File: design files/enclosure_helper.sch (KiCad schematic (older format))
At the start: 42 parts, among them J1 PSU_CON, J11 FLASH_JUMPER, J2 UART_CON, J3 LED_BTN, J4 FAN_CON, J5 PSU_BTN, J6 FAN_BTN, J7 POW_CON, J8 LED_FAN_POW_CON, J9 LED_CON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

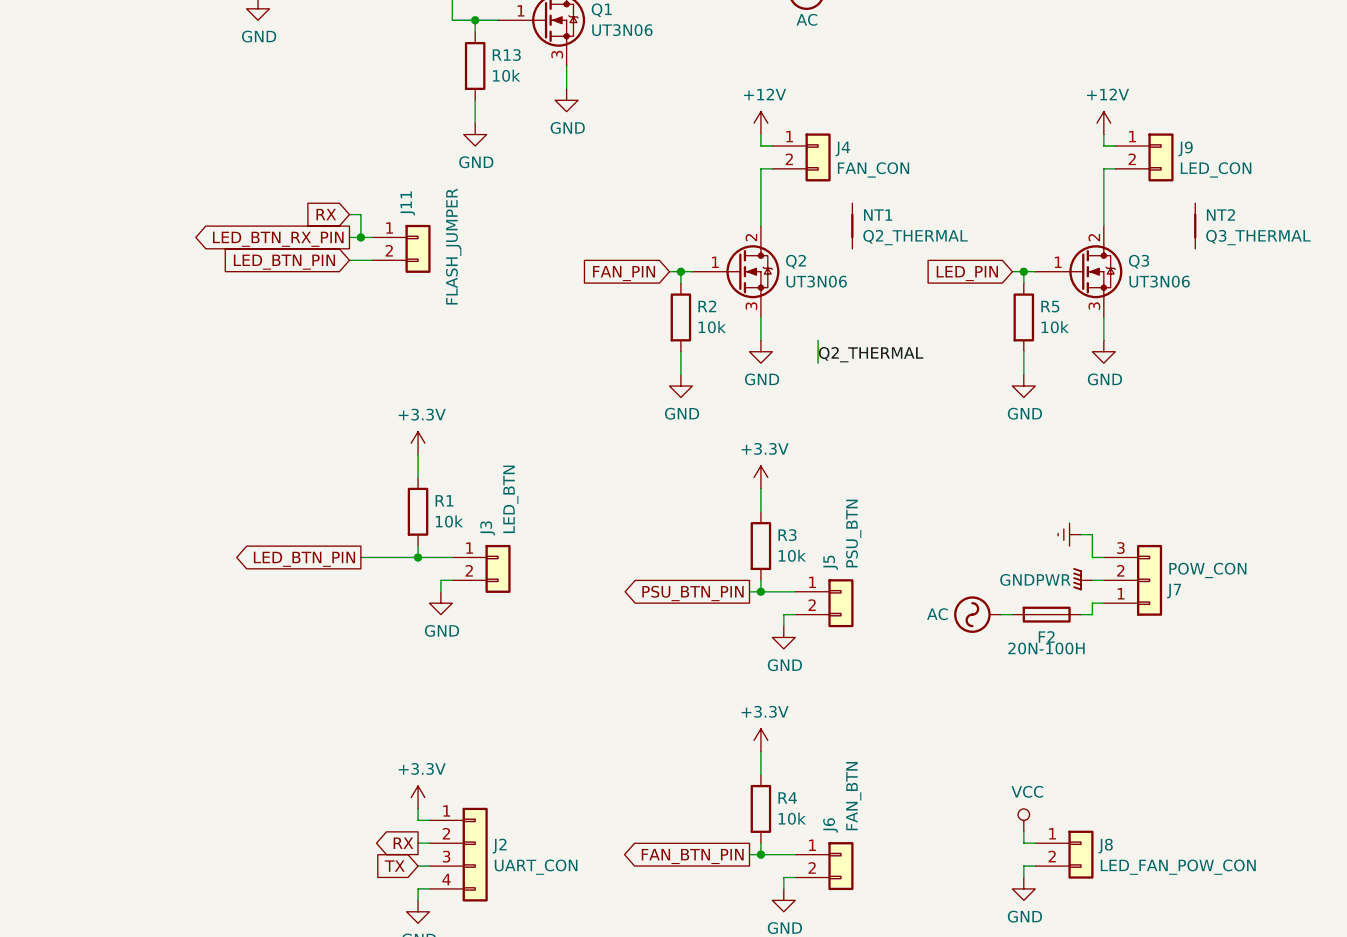
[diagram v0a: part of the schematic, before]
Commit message: Add varistor for mains, add high voltage warning
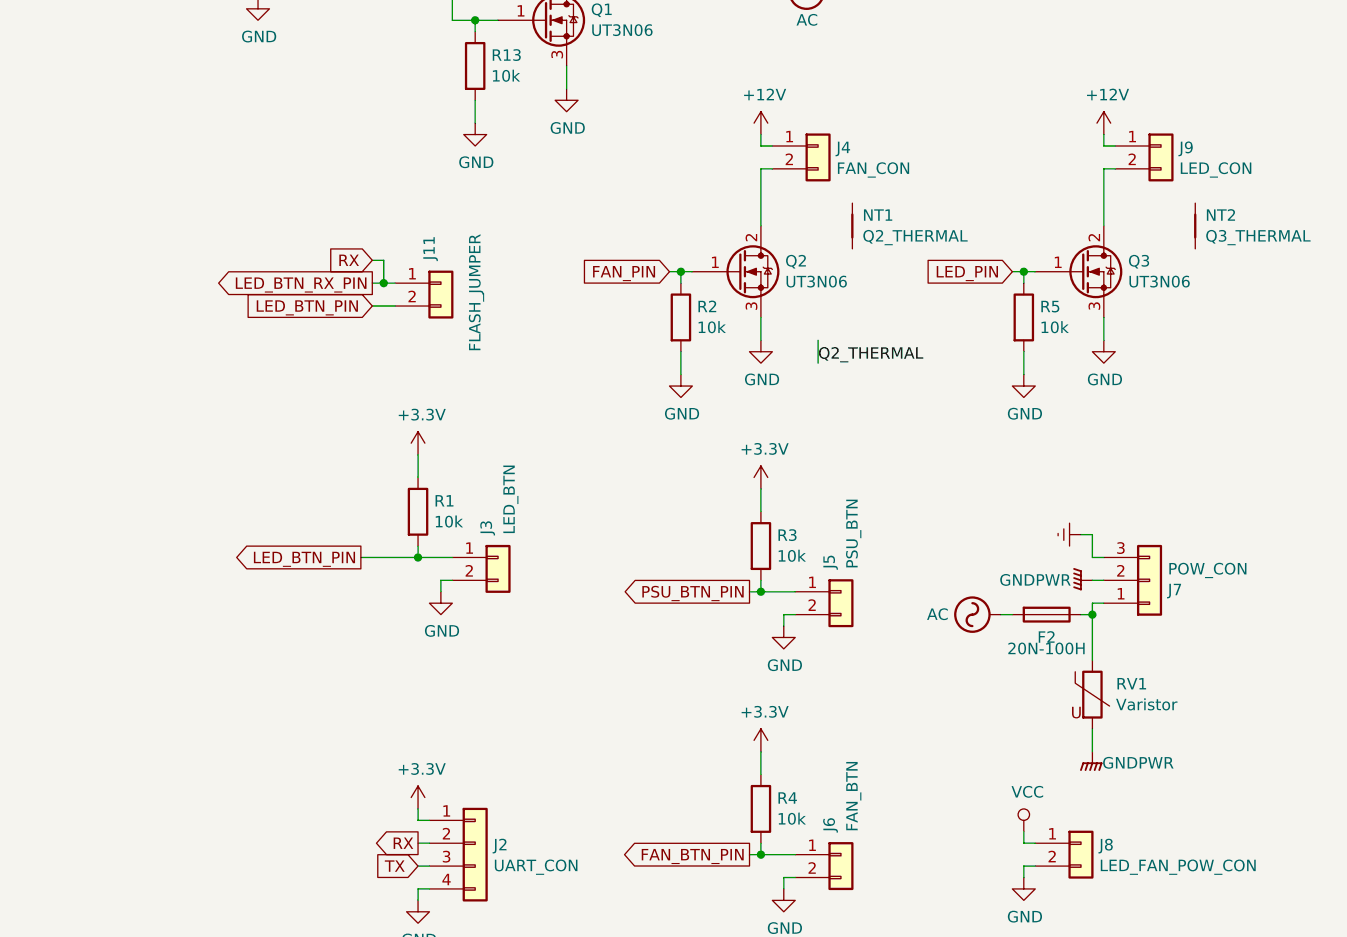
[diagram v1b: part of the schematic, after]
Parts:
- added RV1: Varistor, Varistor:RV_Disc_D12mm_W6.7mm_P7.5mm, symbol Device:Varistor
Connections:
- net GNDPWR: now also RV1.2
- net at F2.1, J7.1 (Pin_1): now also RV1.1
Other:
- moved on the sheet: J11
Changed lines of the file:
@@
 	8300 3200 8350 3200
 Connection ~ 8350 3200
-Text GLabel 6900 3050 0    50   Output ~ 0
+Text GLabel 7000 3250 0    50   Output ~ 0
 LED_BTN_RX_PIN
 Text GLabel 8650 5750 0    50   Output ~ 0
@@
 Wire Wire Line
 	7250 5800 7200 5800
-Text GLabel 6900 2950 0    50   Input ~ 0
+Text GLabel 7000 3150 0    50   Input ~ 0
 RX
 Text GLabel 4300 2950 2    50   Output ~ 0
@@
 Text GLabel 6950 4450 0    50   Output ~ 0
 LED_BTN_PIN
-Text GLabel 6900 3150 0    50   Input ~ 0
+Text GLabel 7000 3350 0    50   Input ~ 0
 LED_BTN_PIN
 Wire Wire Line
-	7000 3150 6900 3150
-Wire Wire Line
-	7000 3050 6950 3050
+	7100 3350 7000 3350
+Wire Wire Line
+	7100 3250 7050 3250
 $Comp
 L Connector_Generic:Conn_01x02 J5
@@
 L Connector_Generic:Conn_01x02 J11
 U 1 1 5F5C880D
-P 7200 3050
-F 0 "J11" V 7150 3150 50  0000 L CNN
-F 1 "FLASH_JUMPER" V 7350 2750 50  0000 L CNN
-F 2 "Connector_PinHeader_2.54mm:PinHeader_1x02_P2.54mm_Vertical" H 7200 3050 50  0001 C CNN
-F 3 "~" H 7200 3050 50  0001 C CNN
-F 4 "https://lcsc.com/product-detail/Pin-Header-Female-Header_Amphenol-ICC_77311-102-02LF_Amphenol-ICC-77311-102-02LF_C180247.html" V 7200 3050 50  0001 C CNN "Link"
-	1    7200 3050
-	1    0    0    -1
-$EndComp
-Wire Wire Line
-	6950 3050 6950 2950
-Wire Wire Line
-	6950 2950 6900 2950
-Connection ~ 6950 3050
-Wire Wire Line
-	6950 3050 6900 3050
+P 7300 3250
+F 0 "J11" V 7250 3350 50  0000 L CNN
+F 1 "FLASH_JUMPER" V 7450 2950 50  0000 L CNN
+F 2 "Connector_PinHeader_2.54mm:PinHeader_1x02_P2.54mm_Vertical" H 7300 3250 50  0001 C CNN
+F 3 "~" H 7300 3250 50  0001 C CNN
+F 4 "https://lcsc.com/product-detail/Pin-Header-Female-Header_Amphenol-ICC_77311-102-02LF_Amphenol-ICC-77311-102-02LF_C180247.html" V 7300 3250 50  0001 C CNN "Link"
+	1    7300 3250
+	1    0    0    -1
+$EndComp
+Wire Wire Line
+	7050 3250 7050 3150
+Wire Wire Line
+	7050 3150 7000 3150
+Connection ~ 7050 3250
+Wire Wire Line
+	7050 3250 7000 3250
 $Comp
 L Device:D_Schottky D1
@@
 	1    0    0    -1
 $EndComp
+$Comp
+L Device:Varistor RV1
+U 1 1 5F59C28E
+P 10150 5050
+F 0 "RV1" H 10253 5096 50  0000 L CNN
+F 1 "Varistor" H 10253 5005 50  0000 L CNN
+F 2 "Varistor:RV_Disc_D12mm_W6.7mm_P7.5mm" V 10080 5050 50  0001 C CNN
+F 3 "~" H 10150 5050 50  0001 C CNN
+F 4 "https://lcsc.com/product-detail/Varistors_RUILON-Shenzhen-Ruilongyuan-Elec-10D471K_C8760.html" H 10150 5050 50  0001 C CNN "Link"
+	1    10150 5050
+	1    0    0    -1
+$EndComp
+$Comp
+L power:GNDPWR #PWR0141
+U 1 1 5F59E17A
+P 10150 5300
+F 0 "#PWR0141" H 10150 5100 50  0001 C CNN
+F 1 "GNDPWR" H 10350 5250 50  0000 C CNN
+F 2 "" H 10150 5250 50  0001 C CNN
+F 3 "" H 10150 5250 50  0001 C CNN
+	1    10150 5300
+	1    0    0    -1
+$EndComp
+Wire Wire Line
+	10150 4700 10150 4900
+Connection ~ 10150 4700
+Wire Wire Line
+	10150 5200 10150 5300
 $EndSCHEMATC
